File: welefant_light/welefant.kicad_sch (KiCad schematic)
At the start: 103 parts, among them J1 Conn_01x02, J2 Conn_02x7_Odd_Even, J3 Conn_02x6_Odd_Even, Q1 AO3401A, Q2 AO3401A, Q3 AO3401A, SW1 ON-OFF, SW2 RESET, SW3 BOOT, SW4 GPIO33, SW5 IO34, U1 RT9080-33GJ5, U2 Audio Jack PJ-324, U3 SD18OB261-060, U4 TP4056, U5 welefant, U6 128MBit Flash, U7 ESP32-S3, U8 Reset 2.8V, X1 40 MHz

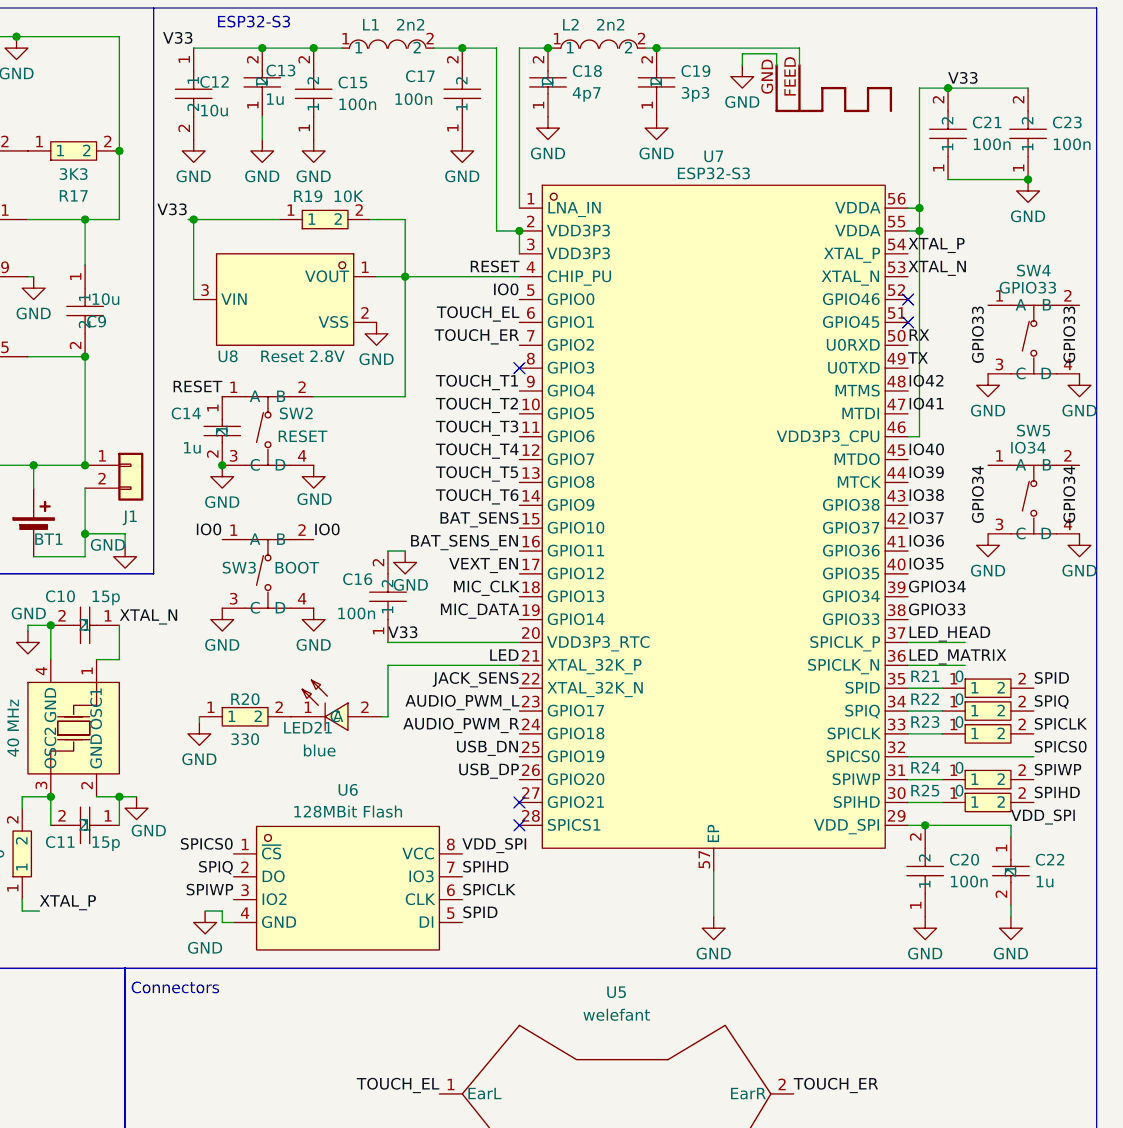
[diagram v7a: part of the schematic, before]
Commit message: use S3FH4R2 / remove flash chip
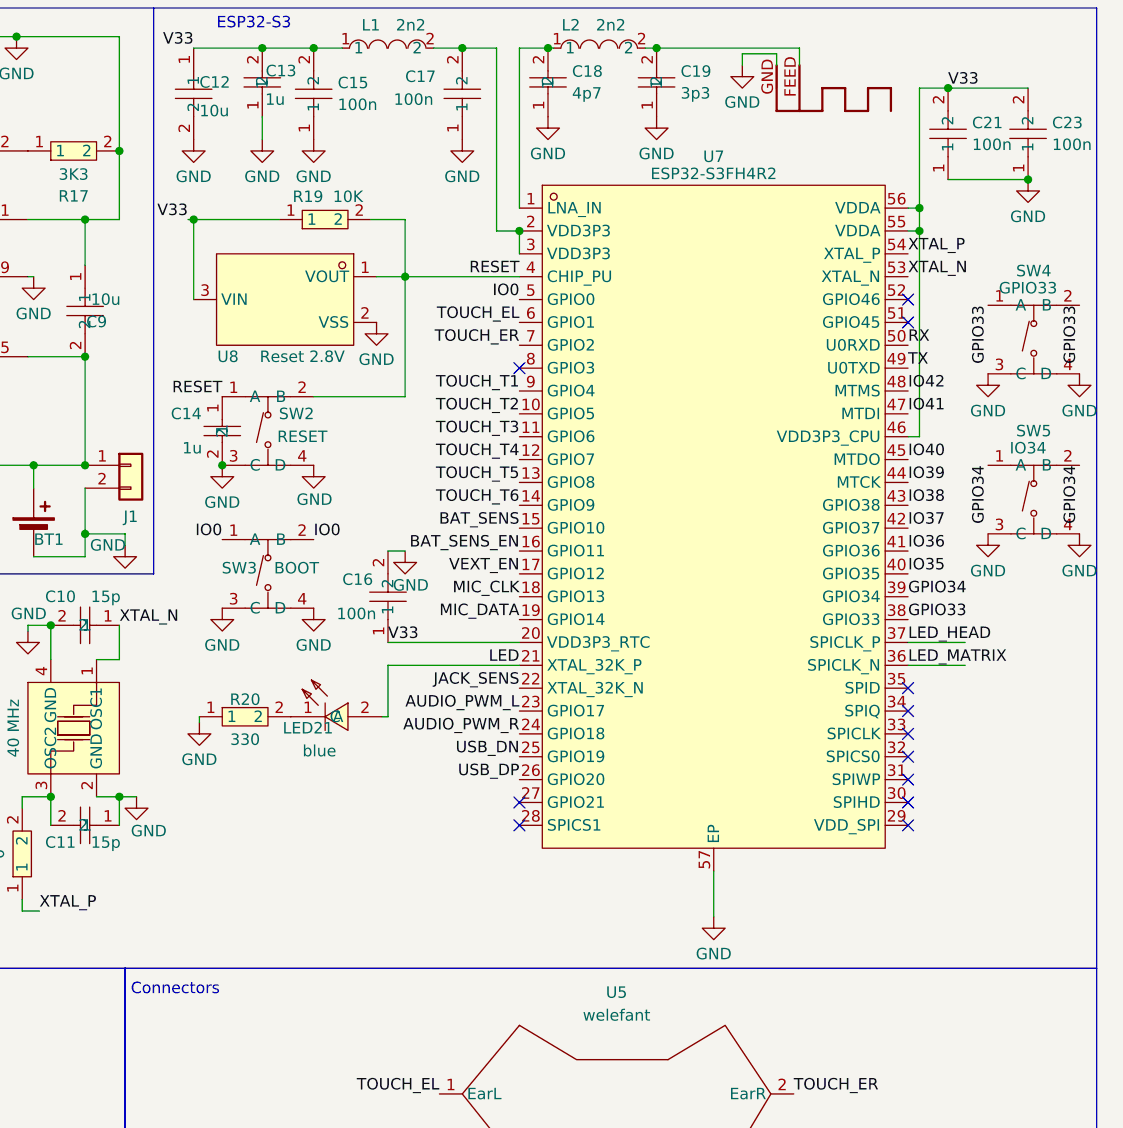
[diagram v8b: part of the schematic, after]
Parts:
- removed C20: 100n, easyeda2kicad:C0603, symbol easyeda2kicad:CC0603KRX7R9BB104
- removed C22: 1u, easyeda2kicad:C0603, symbol easyeda2kicad:CL10A105KB8NNNC
- removed R21, R22, R23, R24, R25: 0, easyeda2kicad:R0603, symbol easyeda2kicad:0603WAF0000T5E
- removed U6: 128MBit Flash, easyeda2kicad:SOIC-8_L5.3-W5.3-P1.27-LS8.0-BL, symbol easyeda2kicad:W25Q128JVSIQTR
- U7: value ESP32-S3 -> ESP32-S3FH4R2; LCSC Part C2913192 -> C3013940
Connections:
- net SPICS0: no longer names the net of U7.32 (SPICS0)
- net VDD_SPI: no longer names the net of U7.29 (VDD_SPI)
- no-connect marks 21 -> 28
